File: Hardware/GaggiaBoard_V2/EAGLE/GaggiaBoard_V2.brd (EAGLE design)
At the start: 102 x 92 mm, 115 parts, among them IC1 LD117AS33TR, J1 4PIN, J11 PIN262409-1, J12 PIN262409-1, J13 PIN262409-1, J14 PIN262409-1, J15 PIN262409-1, J16 PIN262409-1, J17 PIN262409-1, J18 PIN262409-1, J19 PIN262409-1, J2 Vertical Qwiic Connector, J20 PIN262409-1, J3 Vertical Qwiic Connector, J5 2PIN, J6 3PIN, J7 3PIN, J8 5PIN, J9 3PIN, K1 RELAY-SPDT-JZC-11F, K2 RELAY-SPDT-JZC-11F, K3 AQH213, Q1 600mA/40V, Q10 600mA/40V, Q2 600mA/40V, Q3 600mA/40V, Q4 600mA/40V, Q5 600mA/40V, Q6 600mA/40V, Q8 600mA/40V, Q9 600mA/40V, U1 BLACKPILL, U2 MAX31855K, U5 TXS0102

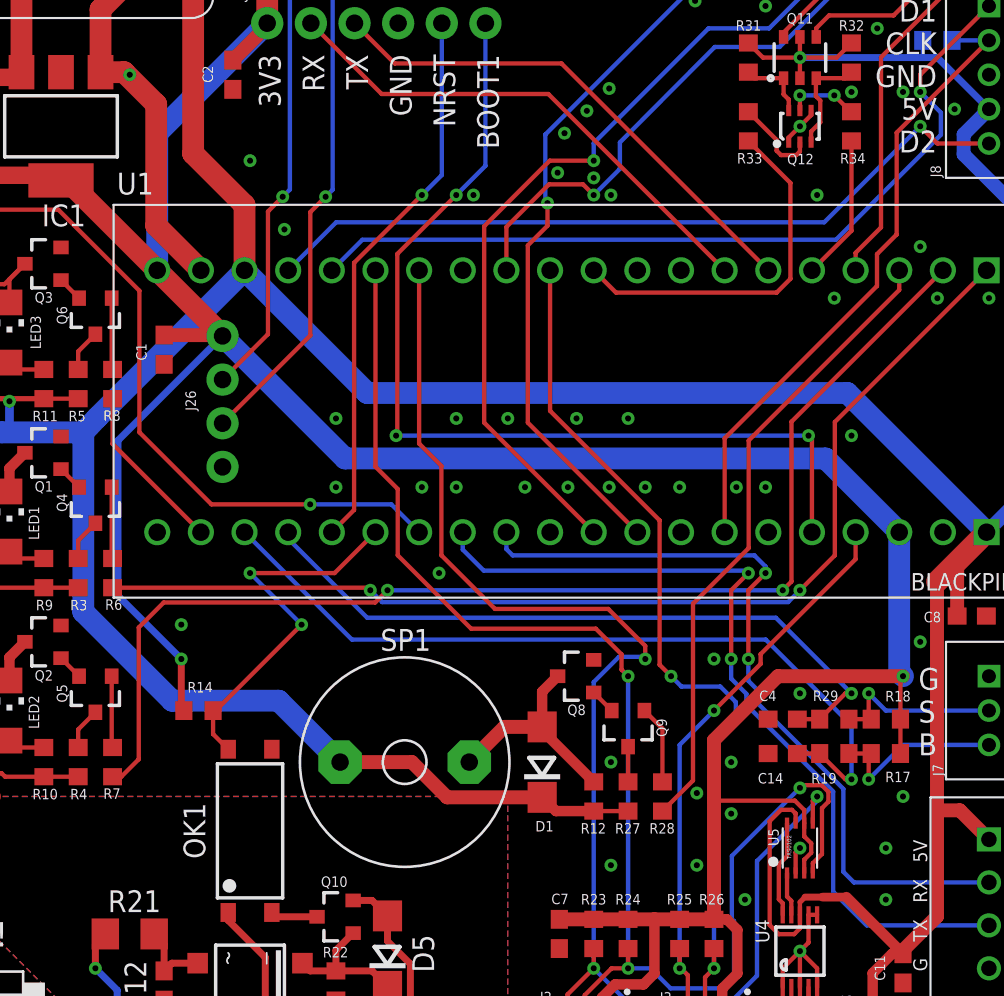
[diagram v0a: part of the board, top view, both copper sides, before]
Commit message: pull downs on GPIO outputs
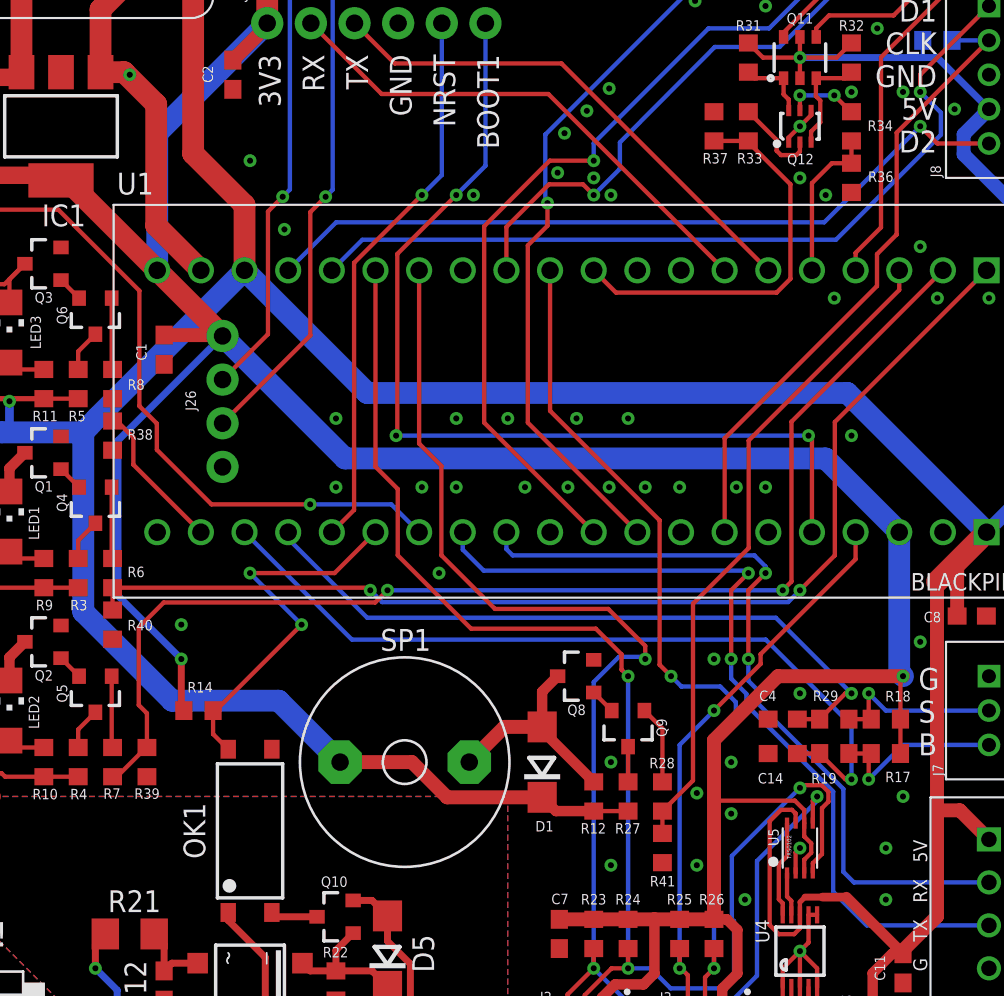
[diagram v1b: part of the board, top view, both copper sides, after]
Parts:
- added R36, R37, R38, R39, R40, R41: 3K3, rcl:R0603
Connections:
- net GND: now also R36.1, R37.1, R38.1, R39.1, R40.1, R41.1
- net PA15: now also R37.2
- net PA8: now also R36.2
- net PB12: now also R40.2
- net PB13: now also R39.2
- net PB14: now also R41.2
- net PC13: now also R38.2
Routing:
- net PA15: track 21.4 -> 23.4 mm
- net PB14: track 37.2 -> 38.5 mm
- net PB12: track 63.8 -> 65.1 mm
- net PA8: track 8.48 -> 9.15 mm
- net GND: vias 81 -> 82
